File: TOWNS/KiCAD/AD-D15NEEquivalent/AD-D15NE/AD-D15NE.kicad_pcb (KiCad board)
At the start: 2 copper layers, 24 x 40.4 mm, 2 parts, among them J2 DE15_Receptacle_HighDensity_M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, J3 DA15_Plug_MountingHoles

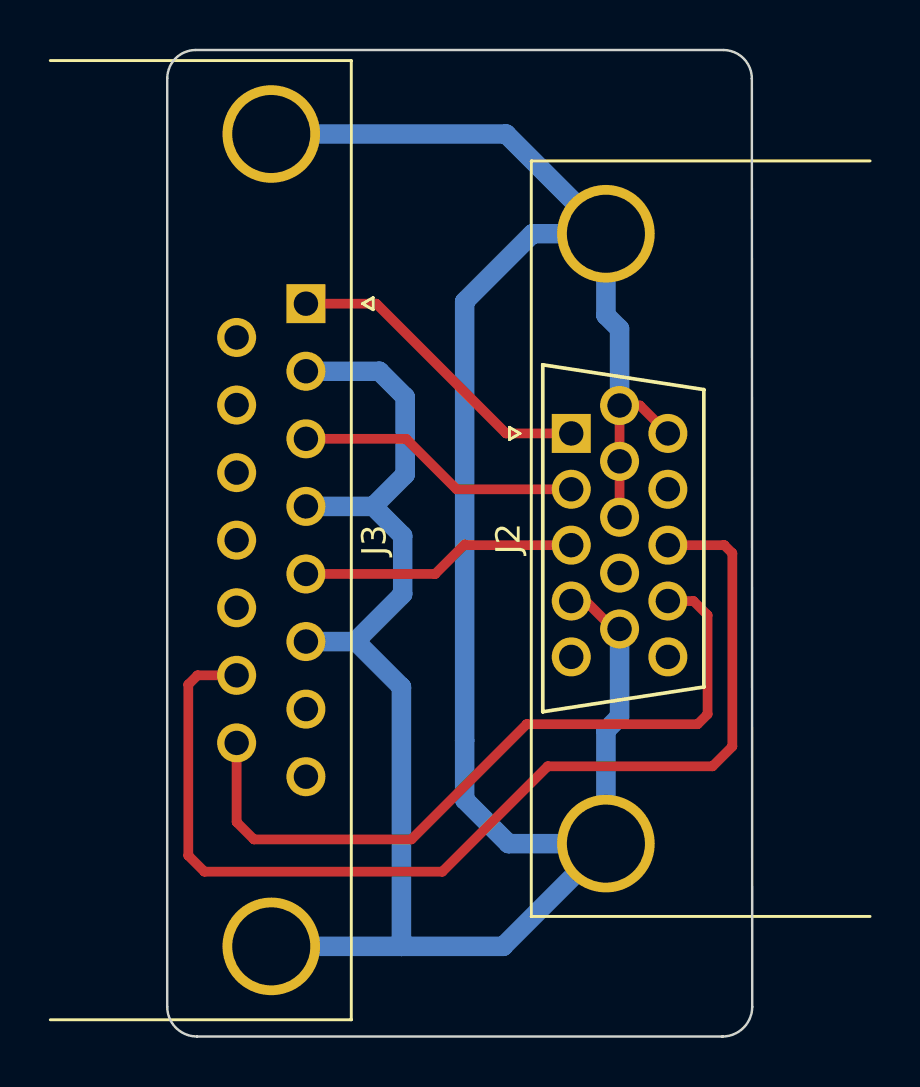
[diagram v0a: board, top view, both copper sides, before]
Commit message: Updated video adapter PCB.
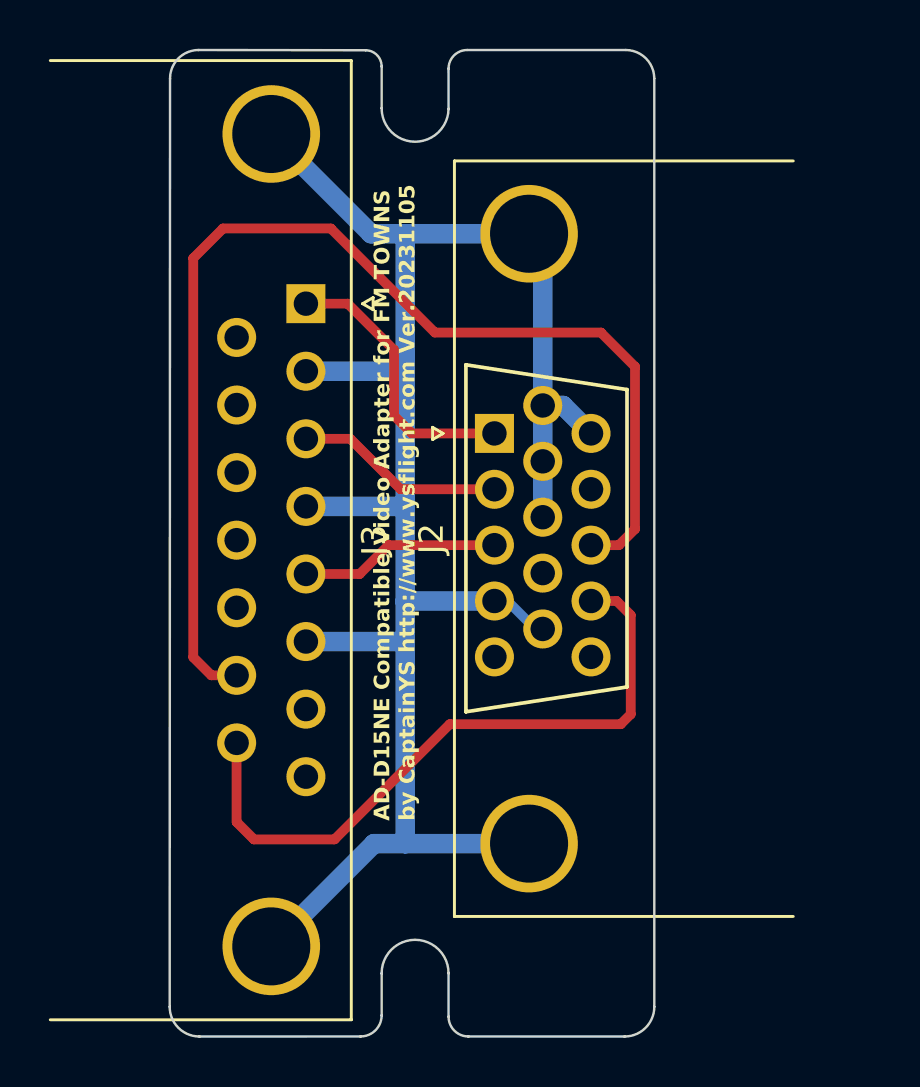
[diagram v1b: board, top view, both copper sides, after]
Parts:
- moved J2 3.15 mm to (143.3, 94.3)
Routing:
- net /Gnd: track 127.1 -> 82.2 mm
- net /HSync: track 44.6 -> 48.1 mm
- net /Green: track 11.7 -> 8.58 mm
- net /VSync: track 30.9 -> 27.8 mm
- net /Blue: track 11.4 -> 8.26 mm
- net /Red: track 13.1 -> 11.5 mm
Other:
- board size 24 x 40.4 mm -> 19.9 x 40.4 mm
- board text added: "AD-D15NE Compatible Video Adapter for FM TOWNS by CaptainYS http://www.ysflight.com Ver.20231105"
